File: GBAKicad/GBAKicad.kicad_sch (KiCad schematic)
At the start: 0 parts

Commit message: Big parts schematic
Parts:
- added A1: RaspberryPi_Pico, Module:RaspberryPi_Pico_Common_Unspecified, symbol MCU_Module:RaspberryPi_Pico
- added BT1: Battery, symbol Device:Battery
- added J1: USB_C_Receptacle_USB2.0_16P, symbol Connector:USB_C_Receptacle_USB2.0_16P
- added J2: Micro_SD_Card_Det1, symbol Connector:Micro_SD_Card_Det1
- added J3: AudioJack3_SwitchT, symbol Connector_Audio:AudioJack3_SwitchT
- added LS1: Speaker, symbol Device:Speaker
- added R1, R10, R2, R3, R4, R5, R6, R7, R8, R9: 10k, symbol Device:R
- added SW1, SW10, SW2, SW3, SW4, SW5, SW6, SW7, SW8, SW9: SW_Push, symbol Switch:SW_Push
- added SW11: SW_SPDT, symbol Switch:SW_SPDT
- added U1: TFT_320x240, z_Devices:TFT-320x240, symbol tft_320x240:TFT_320x240
- added U2: XC6220B331MR, Package_TO_SOT_SMD:SOT-23-5, symbol Regulator_Linear:XC6220B331MR
- added U3: TP4056-42-ESOP8, Package_SO:SOIC-8-1EP_3.9x4.9mm_P1.27mm_EP2.41x3.3mm_ThermalVias, symbol Battery_Management:TP4056-42-ESOP8
- added U4: MAX17048, Package_DFN_QFN:DFN-8-1EP_2x2mm_P0.5mm_EP0.7x1.3mm, symbol PCM_marbastlib-various:MAX17048
- added U5: PCM5102A, Package_SO:TSSOP-20_4.4x6.5mm_P0.65mm, symbol Audio:PCM5102A
- added U6: TPA2012D2RTJR, TPA2012D2RTJR:QFN50P400X400X80-21N270X270, symbol TPA2012D2RTJR:TPA2012D2RTJR
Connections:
- new net: A1.13 (GND), A1.18 (GND), A1.23 (GND), A1.28 (GND), A1.3 (GND), A1.38 (GND), A1.8 (GND)
- new net: J1.A1 (GND), J1.A12 (GND), J1.B1 (GND), J1.B12 (GND)
- new net: J1.A4 (VBUS), J1.A9 (VBUS), J1.B4 (VBUS), J1.B9 (VBUS)
- new net +3V3: R1.1, R10.1, R2.1, R3.1, R4.1, R5.1, R6.1, R7.1, R8.1, R9.1
- new net BTN-R: R10.2, SW10.1
- new net BTN_A: R5.2, SW5.1
- new net BTN_B: R6.2, SW6.1
- new net BTN_L: R9.2, SW9.1
- new net BTN_SELECT: R7.2, SW7.1
- new net BTN_START: R8.2, SW8.1
- new net D_DOWN: R4.2, SW4.1
- new net D_LEFT: R2.2, SW2.1
- new net D_RIGHT: R1.2, SW1.1
- new net D_UP: R3.2, SW3.1
- new net GND: SW1.2, SW10.2, SW2.2, SW3.2, SW4.2, SW5.2, SW6.2, SW7.2, SW8.2, SW9.2
- new net PGND: U6.12 (PGND), U6.4 (PGND)
- new net PVDD: U6.13 (PVDD), U6.3 (PVDD)

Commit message: Schematics Basic Connections
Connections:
- net BTN-R: now also A1.12 (GPIO9)
- net BTN_A: now also A1.32 (GPIO27_ADC1)
- net BTN_B: now also A1.34 (GPIO28_ADC2)
- net BTN_SELECT: now also A1.20 (GPIO15)
- net BTN_START: now also A1.25 (GPIO19)
- net D_DOWN: now also A1.31 (GPIO26_ADC0)
- net D_LEFT: now also A1.2 (GPIO1)
- net D_RIGHT: now also A1.1 (GPIO0)
- net D_UP: now also A1.29 (GPIO22)
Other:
- note added: "Audio Chain"
- note added: "Button Matrix"
- note added: "ILI9341 Display"
- note added: "MicroSD Slot"
- note added: "Power!!!"
- note added: "RP-2350"
- note added: "USB-C Port"
- moved on the sheet: BT1, J1, J2, J3, LS1, R1, R10, R2, R3, R4, R5, R6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

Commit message: my god
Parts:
- removed A1: RaspberryPi_Pico, Module:RaspberryPi_Pico_Common_Unspecified, symbol MCU_Module:RaspberryPi_Pico
- added R11, R12: 10k, symbol Device:R
- added R13: R, symbol Device:R
- added U7: ESP32-S3, Package_DFN_QFN:QFN-56-1EP_7x7mm_P0.4mm_EP4x4mm, symbol MCU_Espressif:ESP32-S3
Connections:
- net PGND is gone; now on net GND: U6.12 (PGND), U6.4 (PGND)
- net PVDD is gone; now on net +3V3: U6.13 (PVDD), U6.3 (PVDD)
- net +3V3: now also J2.4 (VDD), U1.1 (VCC), U5.1 (CPVDD), U5.17 (XSMT), U5.20 (DVDD), U5.8 (AVDD), U6.7 (~{SDL}), U6.8 (~{SDR}), U6.9 (AVDD), R11.1, R12.1, R13.1, U7.43 (GPIO38)
- net BTN-R: now also U7.15 (GPIO10)
- net BTN_A: now also U7.10 (GPIO5)
- net BTN_B: now also U7.11 (GPIO6)
- net BTN_L: now also U7.14 (GPIO9)
- net BTN_SELECT: now also U7.12 (GPIO7)
- net BTN_START: now also U7.13 (GPIO8)
- net D_DOWN: now also U7.9 (GPIO4)
- net D_LEFT: now also U7.7 (GPIO2)
- net D_RIGHT: now also U7.6 (GPIO1)
- net D_UP: now also U7.8 (GPIO3)
- net GND: now also J2.6 (VSS), J2.SH (SHIELD), J3.S, U1.2 (GND), U5.10 (DEMP), U5.11 (FLT), U5.12 (SCK), U5.16 (FMT), U5.19 (DGND), U5.3 (CPGND), U5.9 (AGND), U6.1 (G1), U6.15 (G0), U6.17 (INR-), U6.18 (AGND), U6.19 (INL-), U6.20 (INL+), U6.21 (EXP)
- net at U6.11 (OUTR-): now also LS1.2
- net at U6.14 (OUTR+): now also LS1.1
- net AUDIO_R: now reaches U6.16 (INR+)
- net AUDIO_R: now also J3.R, U5.7 (OUTR)
- net AUDIO_L: now reaches J3.T
- net AUDIO_L: now also U5.6 (OUTL)
- net at J3.TN: now also R13.2
- net at J2.1 (DAT2): now also R12.2
- net SD_CS: now reaches J2.2 (DAT3/CD)
- net SD_CS: now also U7.19 (GPIO14)
- net SD_MOSI: now reaches J2.3 (CMD)
- net SD_MOSI: now also U7.16 (GPIO11)
- net SD_CLK: now reaches J2.5 (CLK)
- net SD_CLK: now also U7.17 (GPIO12)
- net SD_MISO: now reaches J2.7 (DAT0)
- net SD_MISO: now also U7.18 (GPIO13)
- net at J2.8 (DAT1): now also R11.2
- net SD_DET: now reaches J2.9 (DET)
- net SD_DET: now also U7.23 (GPIO17)
- net VBUS: now reaches U3.4 (V_{CC})
- net I2S_BCK: now reaches U5.13 (BCK)
- net I2S_BCK: now also U7.24 (GPIO18)
- net I2S_DATA: now reaches U5.14 (DIN)
- net I2S_DATA: now also U7.41 (GPIO36)
- net I2S_LRCK: now reaches U5.15 (LRCK)
- net I2S_LRCK: now also U7.27 (GPIO21)
- net LCD_CS: now reaches U1.3 (CS)
- net LCD_CS: now also U7.32 (SPICS0)
- net LCD_RST: now reaches U1.4 (RST)
- net LCD_RST: now also U7.39 (GPIO34)
- net LCD_DC: now reaches U1.5 (DC)
- net LCD_DC: now also U7.38 (GPIO33)
- net LCD_MOSI: now reaches U1.6 (MOSI)
- net LCD_MOSI: now also U7.35 (SPID)
- net LCD_SCK: now reaches U1.7 (SCK)
- net LCD_SCK: now also U7.33 (SPICLK)
- net LCD_BL: now reaches U1.8 (LED)
- net LCD_BL: now also U7.40 (GPIO35)
- new net: U7.2 (VDD3P3), U7.3 (VDD3P3)
- new net: U7.55 (VDDA), U7.56 (VDDA)
- no-connect marks 0 -> 8
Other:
- note added: "ESP-32 S3"
- note removed: "RP-2350"
- moved on the sheet: J1, J2, J3, LS1, U1, U5, U6

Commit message: Schematic Power
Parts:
- added R14: 1.2k, symbol Device:R
- added R15, R16, R17: 10k, symbol Device:R
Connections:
- net +3V3: now also U2.3 (CE), U2.5 (VOUT), U3.8 (CE), R15.1, R16.1, R17.1
- net GND: now also BT1.2 (-), U2.2 (GND), U3.3 (GND), U3.9 (EPAD), R14.1
- net VBAT: now reaches SW11.1 (A)
- net VBAT: now also U2.1 (VIN), U3.5 (BAT)
- net VBAT_RAW: now reaches SW11.2 (B)
- net VBAT_RAW: now also BT1.1 (+)
- net at U3.1 (TEMP): now also R15.2
- net at U3.2 (PROG): now also R14.2
- net at U3.6 (~{STDBY}): now also R17.2
- net at U3.7 (~{CHRG}): now also R16.2
- no-connect marks 8 -> 9
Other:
- moved on the sheet: SW11, U2, U4

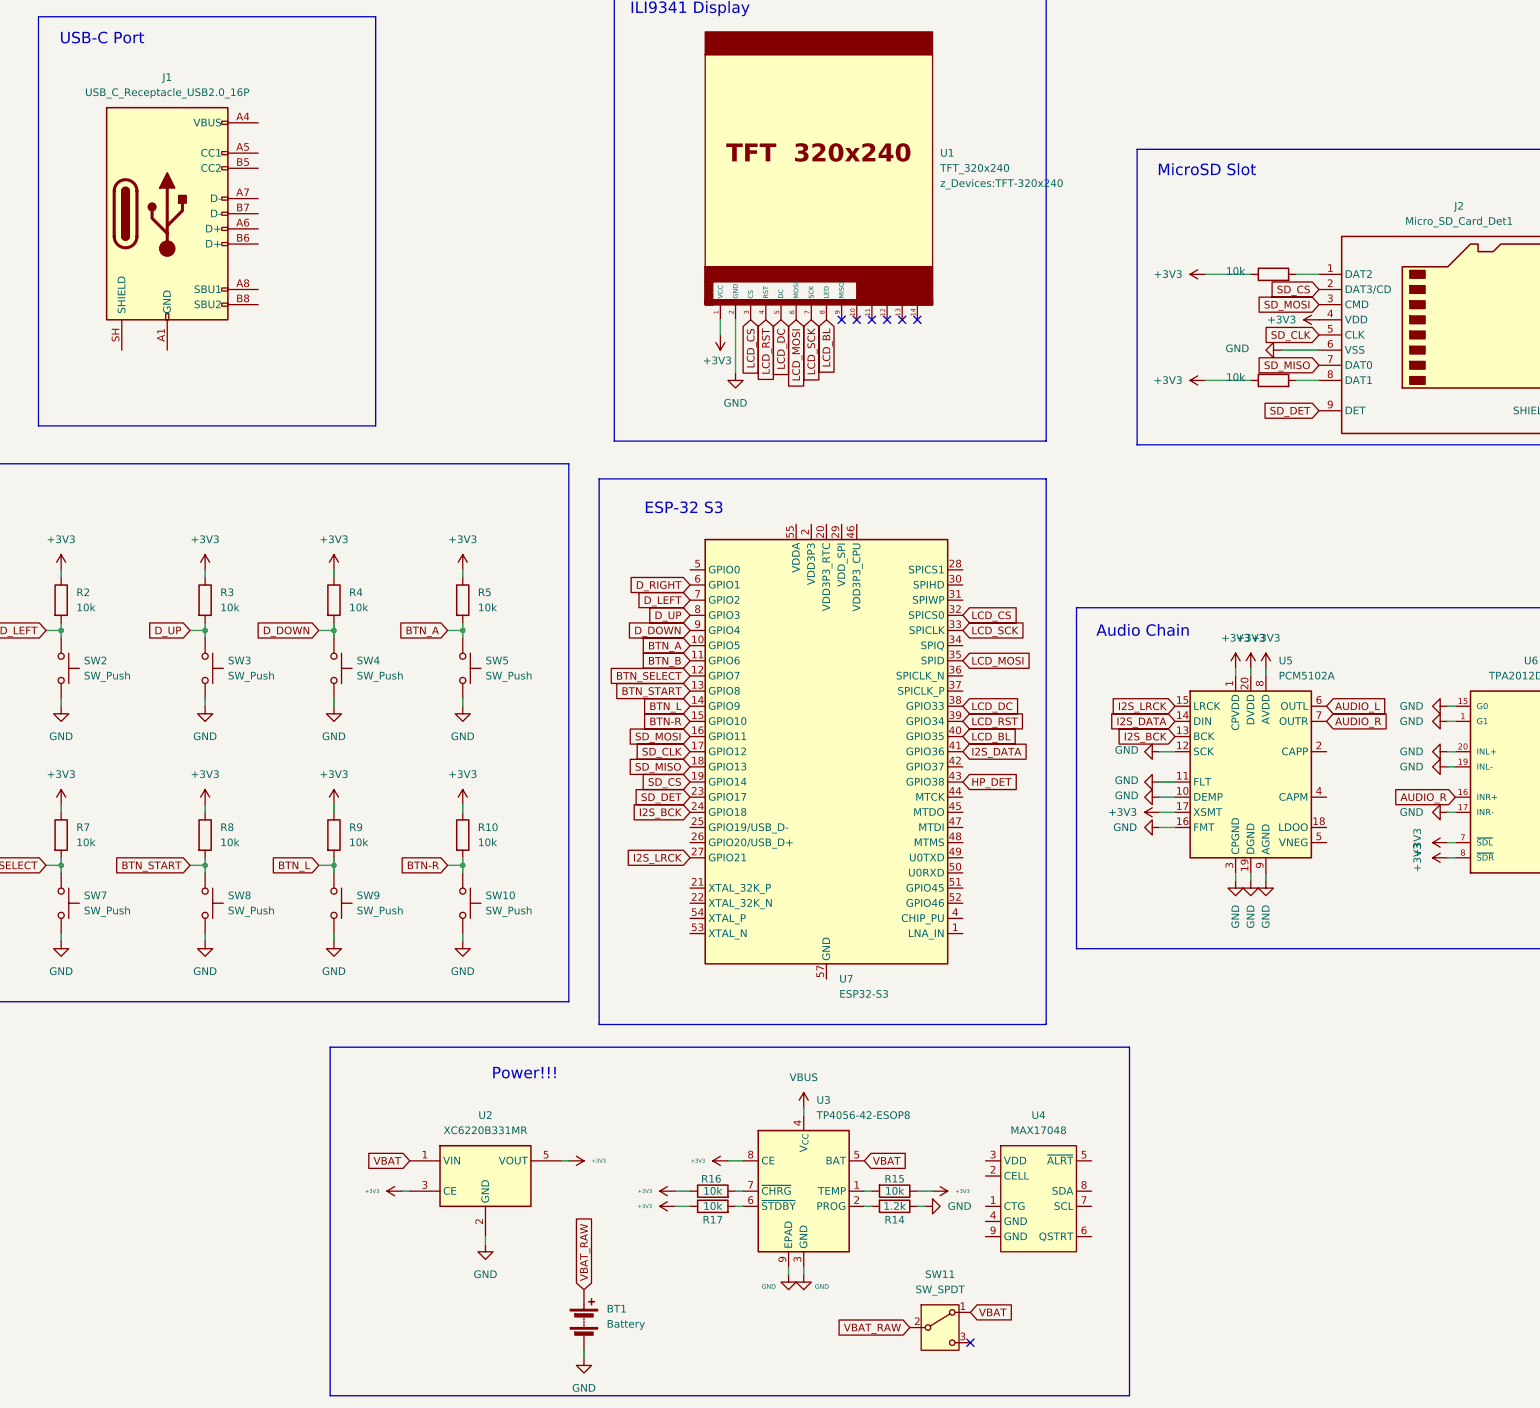
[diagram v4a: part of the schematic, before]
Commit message: usb c schematic
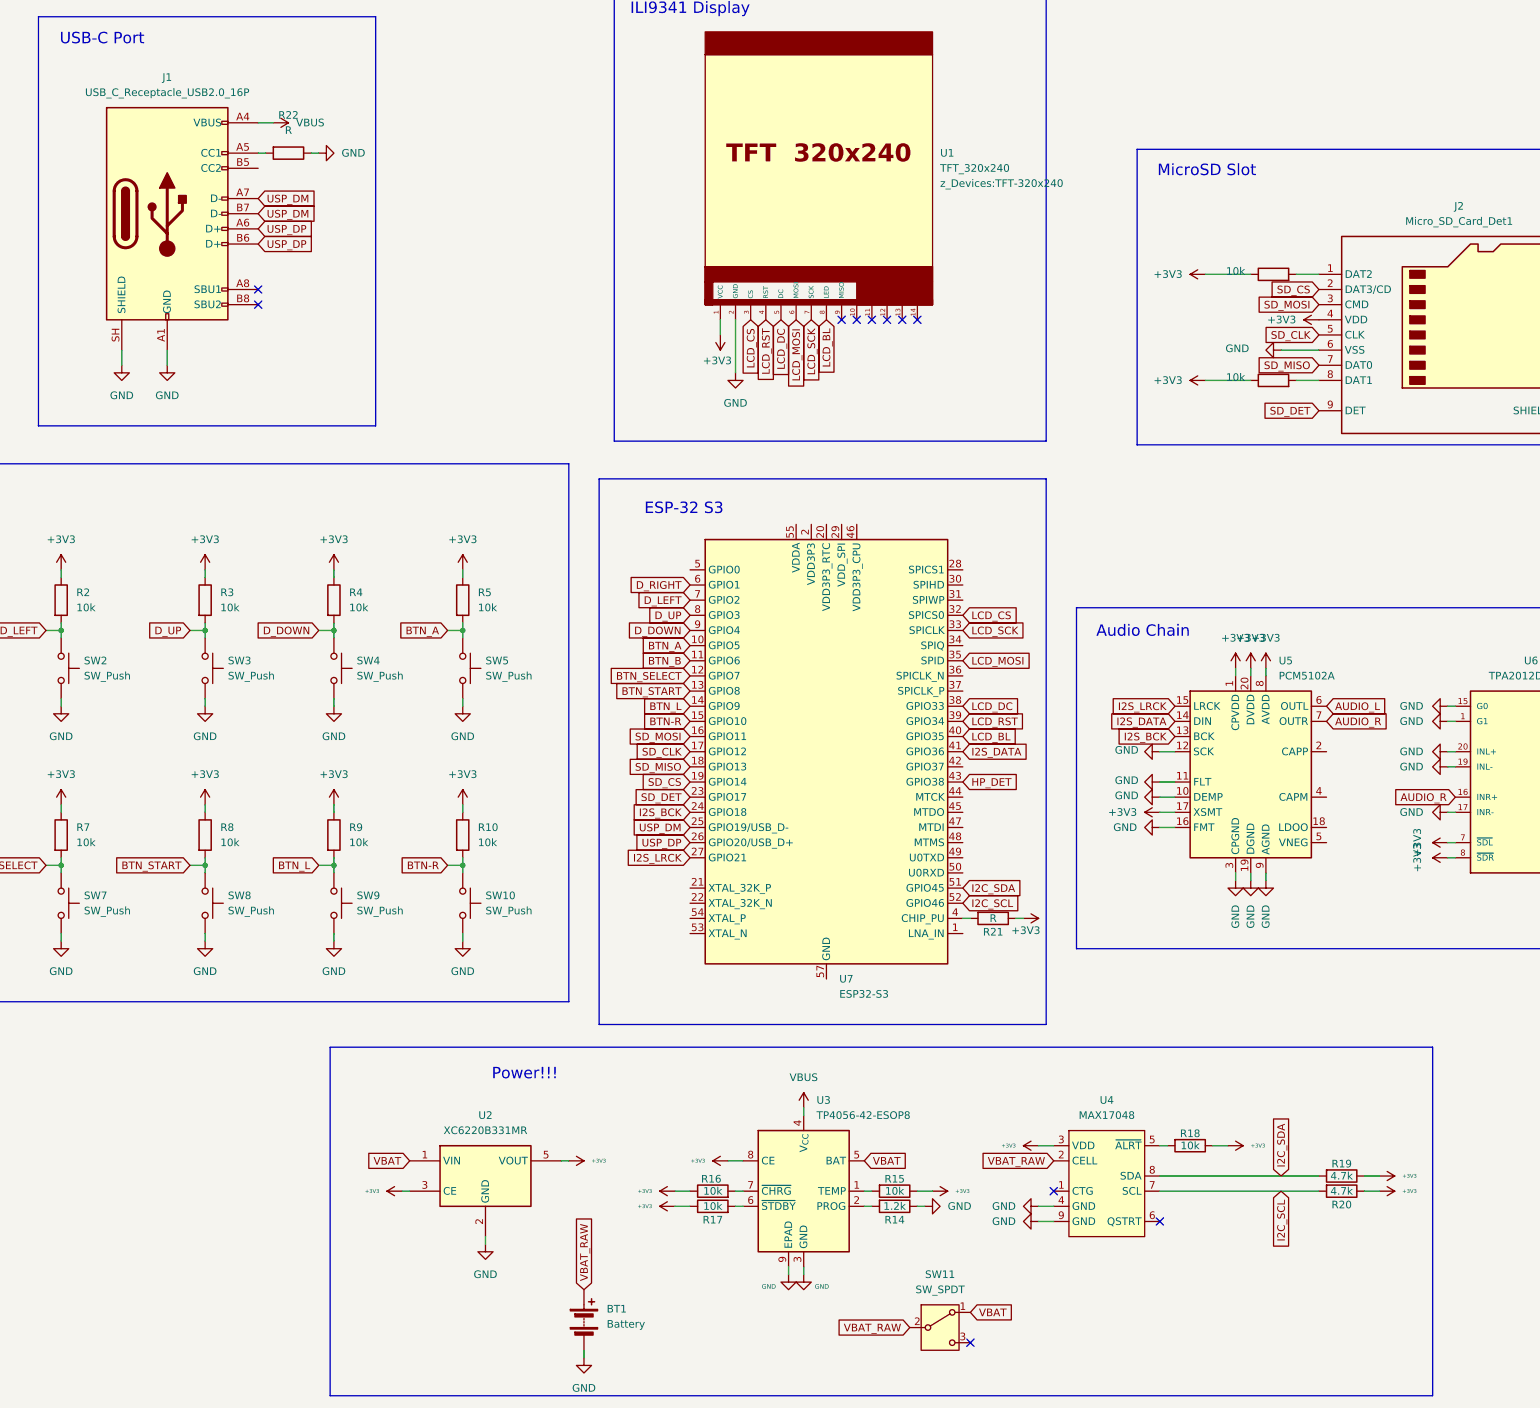
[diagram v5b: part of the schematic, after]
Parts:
- added R18: 10k, symbol Device:R
- added R19, R20: 4.7k, symbol Device:R
- added R21, R22: R, symbol Device:R
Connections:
- net +3V3: now also U4.3 (VDD), R18.1, R19.1, R20.1, R21.1
- net GND: now also J1.A1 (GND), J1.A12 (GND), J1.B1 (GND), J1.B12 (GND), J1.SH (SHIELD), U4.4 (GND), U4.9 (GND), R22.1
- net VBAT_RAW: now also U4.2 (CELL)
- net VBUS: now also J1.A4 (VBUS), J1.A9 (VBUS), J1.B4 (VBUS), J1.B9 (VBUS)
- net at U4.5 (~{ALRT}): now also R18.2
- net I2C_SCL: now reaches U4.7 (SCL)
- net I2C_SCL: now also U7.52 (GPIO46), R20.2
- net I2C_SDA: now reaches U4.8 (SDA)
- net I2C_SDA: now also U7.51 (GPIO45), R19.2
- net USP_DM: now reaches U7.25 (GPIO19/USB_D-)
- net USP_DM: now also J1.A7 (D-), J1.B7 (D-)
- net USP_DP: now reaches U7.26 (GPIO20/USB_D+)
- net USP_DP: now also J1.A6 (D+), J1.B6 (D+)
- net at U7.4 (CHIP_PU): now also R21.2
- net at J1.A5 (CC1): now also R22.2
- no-connect marks 9 -> 13
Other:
- moved on the sheet: U4

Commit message: szematics
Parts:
- R13: value R -> 10k
- R21, R22: value R -> 5.1k
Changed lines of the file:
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@@
 			)
 		)
-		(property "Value" "R"
+		(property "Value" "5.1k"
 			(at 241.3 168.91 90)
 			(show_name no)
@@
 			)
 		)
-		(property "Value" "R"
+		(property "Value" "10k"
 			(at 389.89 157.226 90)
 			(show_name no)
@@
 	)
 	(symbol
+		(lib_name "+3V3_1")
 		(lib_id "power:+3V3")
 		(at 187.96 214.63 90)
@@
 		(in_pos_files yes)
 		(dnp no)
-		(fields_autoplaced yes)
 		(property "Reference" "R22"
-			(at 123.19 34.29 90)
+			(at 123.19 38.354 90)
 			(show_name no)
 			(do_not_autoplace no)
@@
 			)
 		)
-		(property "Value" "R"
-			(at 123.19 36.83 90)
+		(property "Value" "5.1k"
+			(at 123.19 40.64 90)
 			(show_name no)
 			(do_not_autoplace no)

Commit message: Decoupling and error fixing
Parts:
- added C1, C10, C11, C2, C3, C4, C5, C6, C7, C8: 100nF, symbol Device:C
- added C12, C9: 1uF, symbol Device:C
- added R23: 10k, symbol Device:R
- added R24: 100, symbol Device:R
- R21: value 5.1k -> 10k
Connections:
- net +3V3: now also C1.1, C2.1, C3.1, C4.1, C5.1, C6.1, C7.1, C8.1, C9.1, R23.1
- net GND: now also C1.2, C10.2, C11.2, C2.2, C3.2, C4.2, C5.2, C6.2, C7.2, C8.2, C9.2
- net LCD_BL: now also R24.2; no longer U7.40 (GPIO35)
- net VBUS: now also C10.1, C11.1
- net at U7.5 (GPIO0): now also R23.2
- net at U5.2 (CAPP): now also C12.1
- net at U5.4 (CAPM): now also C12.2
- net BTN-R renamed BTN_R
- new net: R24.1, U7.40 (GPIO35)
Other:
- moved on the sheet: R1, R10, R2, R21, R3, R4, R5, R6, R7, R8, R9, SW1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

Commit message: schematic
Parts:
- added R25: 5.1k, symbol Device:R
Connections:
- net +3V3: now also U7.2 (VDD3P3), U7.20 (VDD3P3_RTC), U7.29 (VDD_SPI), U7.3 (VDD3P3), U7.46 (VDD3P3_CPU), U7.55 (VDDA), U7.56 (VDDA)
- net GND: now also U7.57 (GND), R25.1
- net at J1.B5 (CC2): now also R25.2
- no-connect marks 13 -> 31
